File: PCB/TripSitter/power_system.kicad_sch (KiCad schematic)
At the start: 37 parts, among them J4 USB_B_Micro, J5 Jack-DC, SW2 SW_DPDT_x2, SW3 SW_DIP_x05, U2 TPS54325_PWP_14, U5 TPS54294PWP

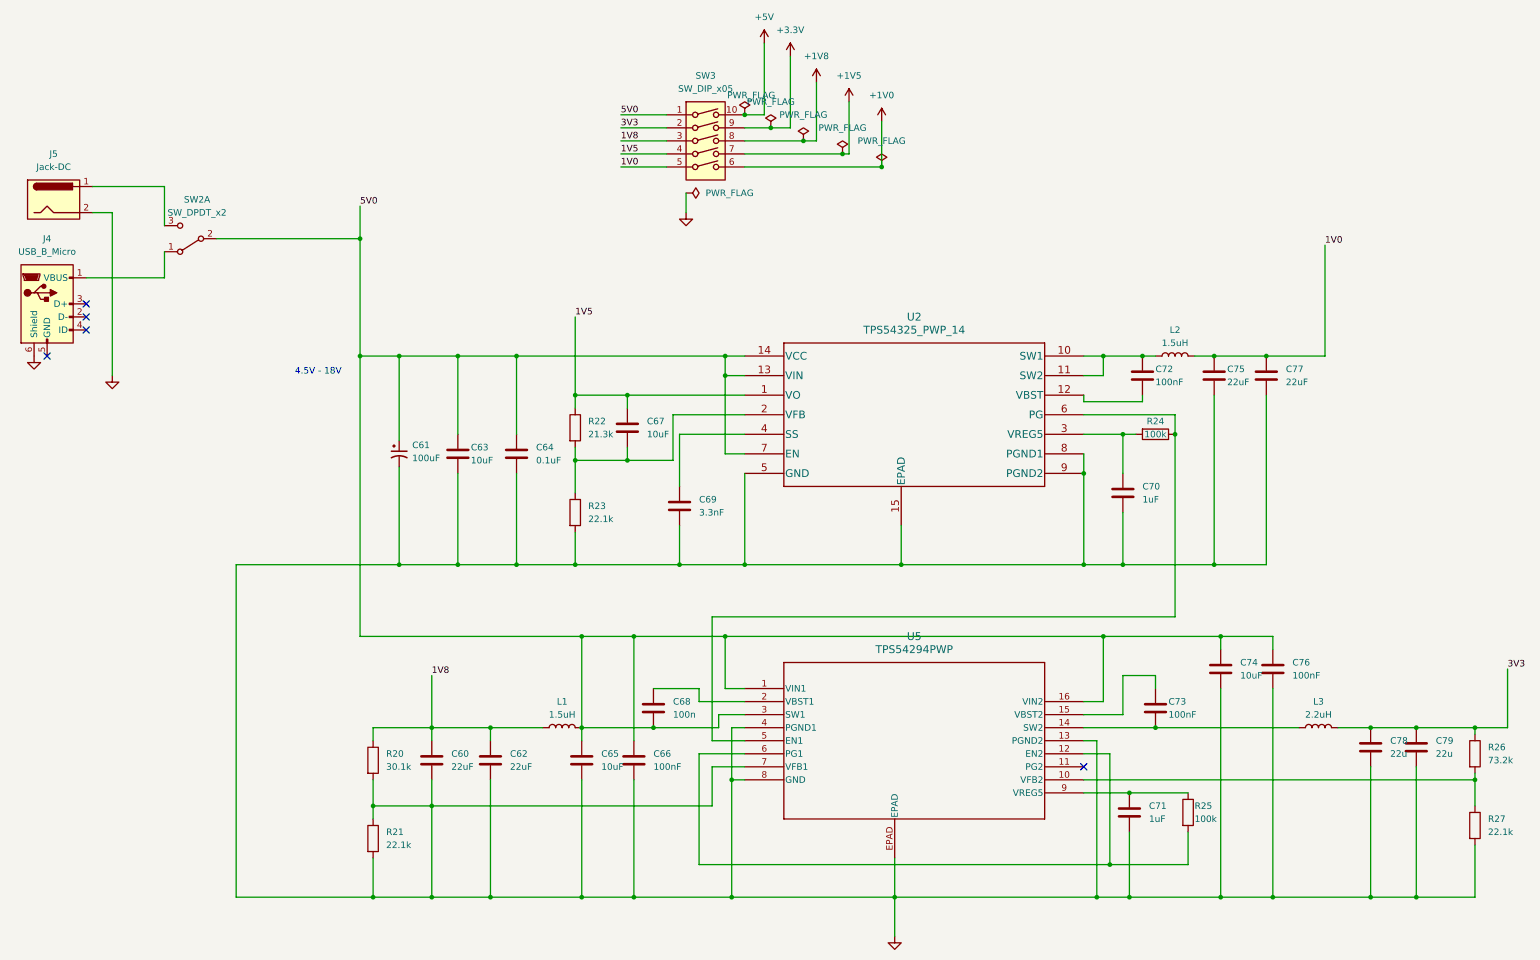
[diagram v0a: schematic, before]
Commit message: pcb: re-structured PCB schematic layout (#17)
Co-authored-by: Sigvart Hovland <sigvart.m@gmail.com>
Co-authored-by: Ida-Sofie Pettersen <idasofie@Ida-Sofies-MacBook-Air.local>
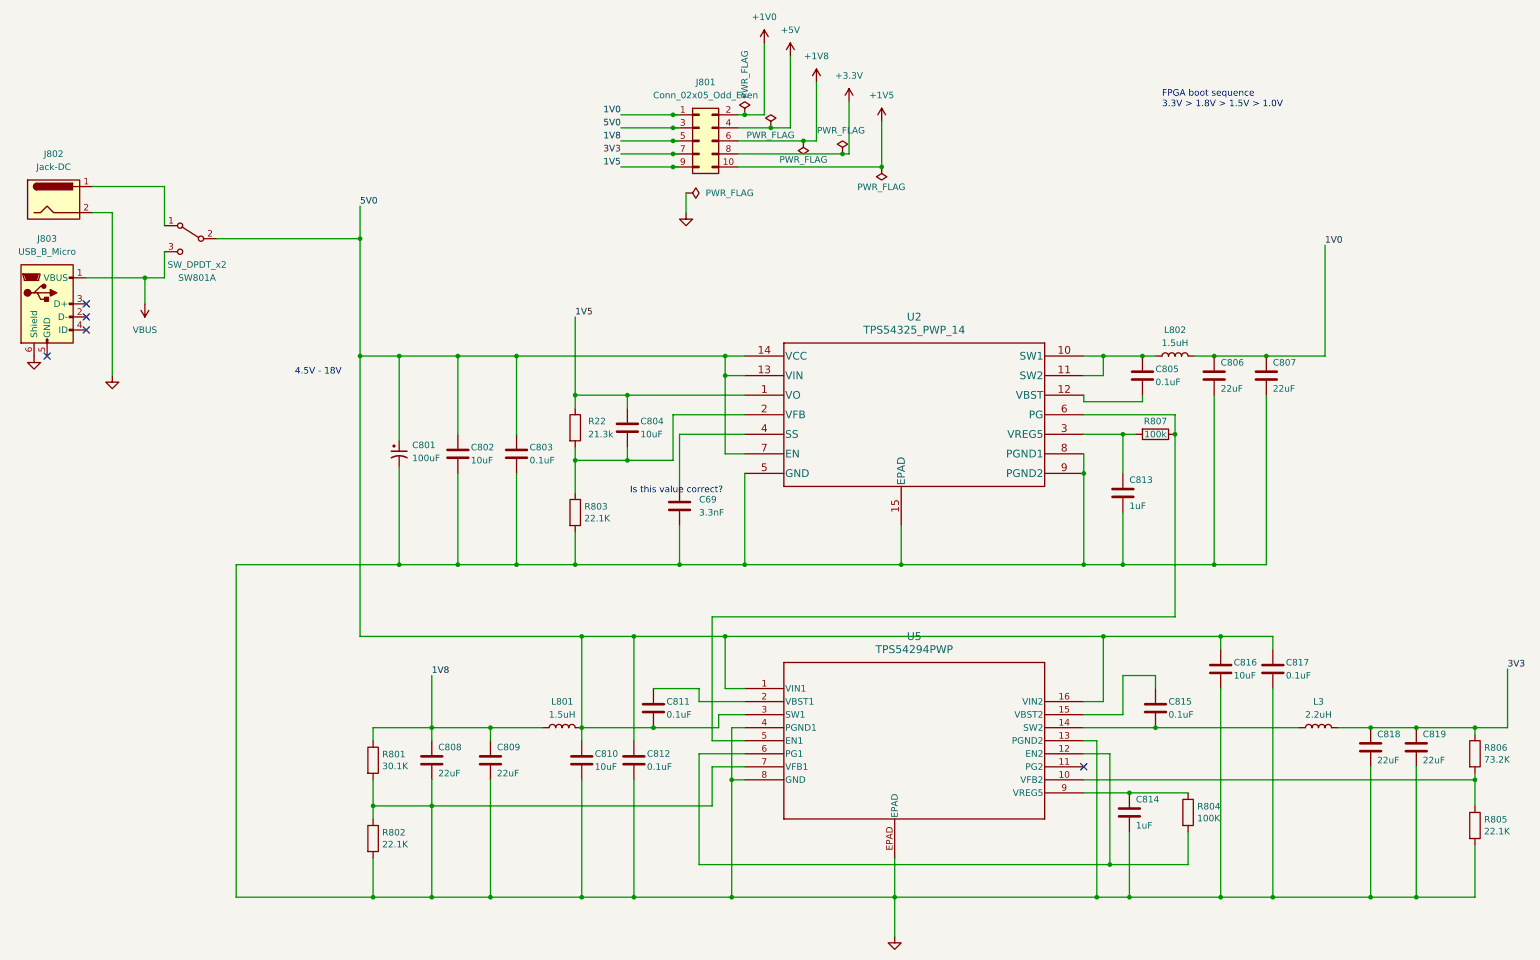
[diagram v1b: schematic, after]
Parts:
- removed C60, C62, C75, C77: 22uF, Capacitor_SMD:C_0402_1005Metric_Pad0.74x0.62mm_HandSolder, symbol Device:C
- removed C64: 0.1uF, Capacitor_SMD:C_0201_0603Metric_Pad0.64x0.40mm_HandSolder, symbol Device:C
- removed C65, C67, C74: 10uF, Capacitor_SMD:C_0402_1005Metric_Pad0.74x0.62mm_HandSolder, symbol Device:C
- removed C66, C72, C73, C76: 100nF, Capacitor_SMD:C_0201_0603Metric_Pad0.64x0.40mm_HandSolder, symbol Device:C
- removed C68: 100n, Capacitor_SMD:C_0201_0603Metric_Pad0.64x0.40mm_HandSolder, symbol Device:C
- removed C70, C71: 1uF, Capacitor_SMD:C_0201_0603Metric_Pad0.64x0.40mm_HandSolder, symbol Device:C
- removed C78, C79: 22u, Capacitor_SMD:C_0402_1005Metric_Pad0.74x0.62mm_HandSolder, symbol Device:C
- removed R20: 30.1k, Resistor_SMD:R_0805_2012Metric_Pad1.20x1.40mm_HandSolder, symbol Device:R
- removed R21, R23, R27: 22.1k, Resistor_SMD:R_0805_2012Metric_Pad1.20x1.40mm_HandSolder, symbol Device:R
- removed R25: 100k, Resistor_SMD:R_0805_2012Metric_Pad1.20x1.40mm_HandSolder, symbol Device:R
- removed R26: 73.2k, Resistor_SMD:R_0805_2012Metric_Pad1.20x1.40mm_HandSolder, symbol Device:R
- removed SW3: SW_DIP_x05, Connector_PinHeader_1.27mm:PinHeader_2x05_P1.27mm_Vertical, symbol Switch:SW_DIP_x05
- added C803, C805, C811, C812, C815, C817: 0.1uF, Capacitor_SMD:C_0603_1608Metric_Pad1.08x0.95mm_HandSolder, symbol Device:C
- added C804, C810, C816: 10uF, Capacitor_SMD:C_0402_1005Metric_Pad0.74x0.62mm_HandSolder, symbol Device:C
- added C806, C807, C808, C809, C818, C819: 22uF, Capacitor_SMD:C_0603_1608Metric_Pad1.08x0.95mm_HandSolder, symbol Device:C
- added C813, C814: 1uF, Capacitor_SMD:C_0402_1005Metric_Pad0.74x0.62mm_HandSolder, symbol Device:C
- added J801: Conn_02x05_Odd_Even, Connector_PinHeader_2.00mm:PinHeader_2x05_P2.00mm_Vertical, symbol Connector_Generic:Conn_02x05_Odd_Even
- added R801: 30.1K, Resistor_SMD:R_0805_2012Metric_Pad1.20x1.40mm_HandSolder, symbol Device:R
- added R802, R803, R805: 22.1K, Resistor_SMD:R_0805_2012Metric_Pad1.20x1.40mm_HandSolder, symbol Device:R
- added R804: 100K, Resistor_SMD:R_0805_2012Metric_Pad1.20x1.40mm_HandSolder, symbol Device:R
- added R806: 73.2K, Resistor_SMD:R_0805_2012Metric_Pad1.20x1.40mm_HandSolder, symbol Device:R
- C69: footprint Capacitor_SMD:C_0402_1005Metric_Pad0.74x0.62mm_HandSolder -> Capacitor_SMD:C_0201_0603Metric_Pad0.64x0.40mm_HandSolder
- C801: renamed from C61; footprint Capacitor_SMD:C_1210_3225Metric_Pad1.33x2.70mm_HandSolder -> Capacitor_SMD:C_0805_2012Metric_Pad1.18x1.45mm_HandSolder; Component Name (none) -> CL21A107MQYNNWE; DK_Ref (none) -> https://www.digikey.no/en/products/detail/samsung-electro-m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
- C802: renamed from C63; Component Name (none) -> CL10A106KQ8NNNC; DK_Ref (none) -> https://www.digikey.no/en/products/detail/samsung-electro-m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
- R807: renamed from R24; Component Name (none) -> RR1220P-104-D; DK_Ref (none) -> https://www.digikey.no/product-detail/no/susumu/RR1220P-104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
- SW801: renamed from SW2; footprint Button_Switch_SMD:SW_DPDT_CK_JS202011JCQN -> Button_Switch_THT:SW_E-Switch_EG1224_SPDT_Angled
- renumbered J5 to J802, J4 to J803, L1 to L801, L2 to L802
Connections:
- net +1V0: now also J801.2 (Pin_2)
- net +1V5: now also J801.10 (Pin_10)
- net +1V8: now also J801.6 (Pin_6)
- net +3.3V: now also J801.8 (Pin_8)
- net +5V: now also J801.4 (Pin_4)
- net 1V0: now also C806.2, C807.2, J801.1 (Pin_1)
- net 1V5: now also C804.1, J801.9 (Pin_9)
- net 1V8: now also C808.2, C809.2, J801.5 (Pin_5), R801.1
- net 3V3: now also C818.2, C819.2, J801.7 (Pin_7), R806.1
- net 5V0: now also C803.1, C810.1, C811.2, C812.1, C816.1, C817.1, J801.3 (Pin_3)
- net GND: now also C803.2, C806.1, C807.1, C808.1, C809.1, C810.2, C812.2, C813.2, C814.2, C816.2, C817.2, C818.1, C819.1, R801.2, R802.1, R802.2, R803.2, R805.2
- net at U5.10 (VFB2): now also R805.1, R806.2
- net at L802.1, U2.10 (SW1), U2.11 (SW2): now also C805.1
- net at U2.12 (VBST): now also C805.2
- net at U5.15 (VBST2): now also C815.1
- net at L3.1, U5.14 (SW2): now also C815.2
- net at U5.12 (EN2), U5.6 (PG1): now also R804.2
- net at U5.2 (VBST1): now also C811.1
- net at U5.9 (VREG5): now also C814.1, R804.1
- net at R22.2, U2.2 (VFB): now also C804.2, R803.1
- net at SW801.1 (A): now also J802.1; no longer J803.1 (VBUS)
- net VBUS: now reaches SW801.3 (C)
- net VBUS: now also J803.1 (VBUS); no longer J802.1
- net at R807.2, U2.3 (VREG5): now also C813.1
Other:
- note added: "FPGA boot sequence 3.3V > 1.8V > 1.5V > 1.0V"
- note added: "Is this value correct?"
- moved on the sheet: SW801A

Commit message: fix power circuit and replace jtag debug
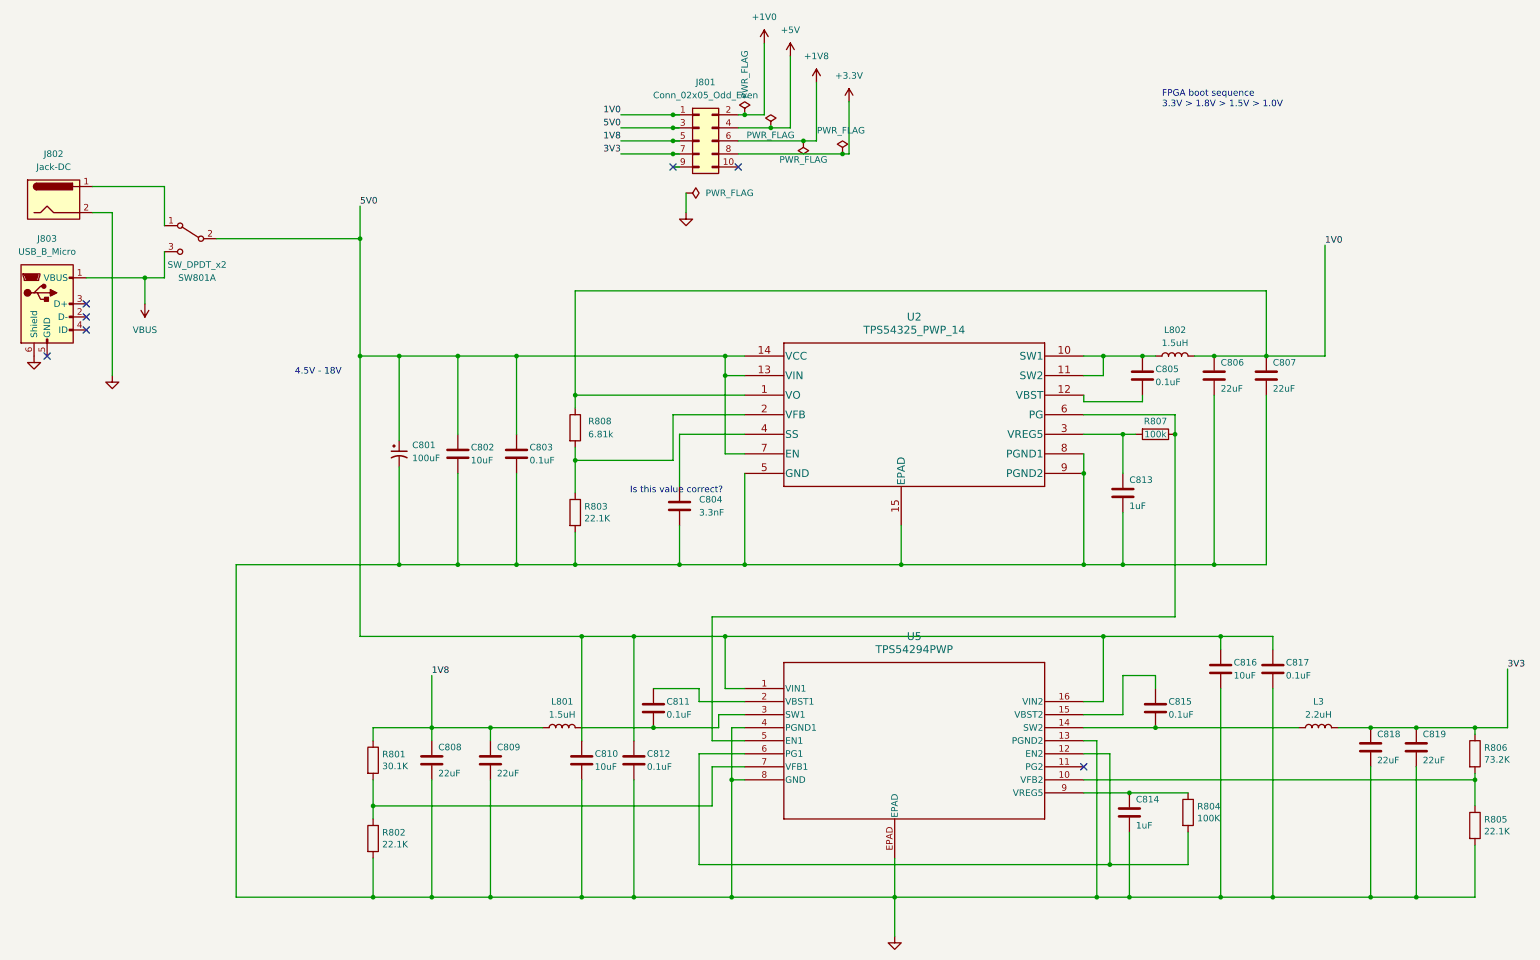
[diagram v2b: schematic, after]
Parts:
- removed C804: 10uF, Capacitor_SMD:C_0402_1005Metric_Pad0.74x0.62mm_HandSolder, symbol Device:C
- R808: renamed from R22; value 21.3k -> 6.81k
- renumbered C69 to C804
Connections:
- net 1V0: now also R808.1, U2.1 (VO)
- net 5V0: no longer C811.2, L801.2, U5.3 (SW1)
- net GND: no longer R801.2, R802.1, U5.7 (VFB1)
- net +1V5: no longer names the net of J801.10 (Pin_10)
- removed net 1V5: J801.9 (Pin_9), R808.1, U2.1 (VO)
- new net: C811.2, L801.2, U5.3 (SW1)
- new net: R801.2, R802.1, U5.7 (VFB1)
- no-connect marks 5 -> 7

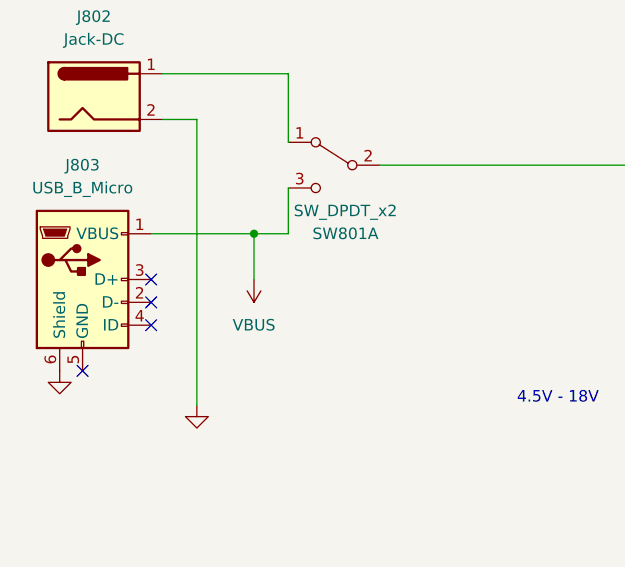
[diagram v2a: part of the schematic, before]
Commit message: fix DRC errors and edit footprint vias
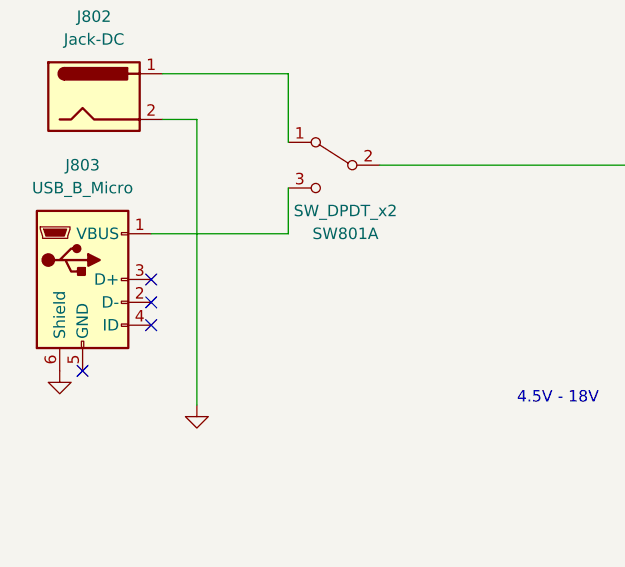
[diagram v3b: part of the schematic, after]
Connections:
- net VBUS: no longer names the net of J803.1 (VBUS), SW801.3 (C)
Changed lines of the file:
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@@
   (junction (at 224.79 217.17) (diameter 0) (color 0 0 0 0)
-  )
-  (junction (at 78.74 96.52) (diameter 0) (color 0 0 0 0)
   )
   (junction (at 317.5 184.15) (diameter 0) (color 0 0 0 0)
@@
     (stroke (width 0) (type default))
   )
-  (wire (pts (xy 67.31 96.52) (xy 78.74 96.52))
-    (stroke (width 0) (type default))
-  )
-  (wire (pts (xy 78.74 96.52) (xy 82.55 96.52))
+  (wire (pts (xy 67.31 96.52) (xy 82.55 96.52))
     (stroke (width 0) (type default))
   )
@@
   )
   (wire (pts (xy 123.19 217.17) (xy 134.62 217.17))
-    (stroke (width 0) (type default))
-  )
-  (wire (pts (xy 78.74 96.52) (xy 78.74 101.6))
     (stroke (width 0) (type default))
   )
@@
         )
       )
-    )
-  )
-  (symbol (lib_id "power:VBUS") (at 78.74 101.6 180) (unit 1)
-    (in_bom yes) (on_board yes) (dnp no) (fields_autoplaced)
-    (property "Reference" "#PWR047" (at 78.74 97.79 0)
-      (effects (font (size 1.27 1.27)) hide)
-    )
-    (property "Value" "VBUS" (at 78.74 106.68 0)
-      (effects (font (size 1.27 1.27)))
-    )
-    (property "Footprint" "" (at 78.74 101.6 0)
-      (effects (font (size 1.27 1.27)) hide)
-    )
-    (property "Datasheet" "" (at 78.74 101.6 0)
-      (effects (font (size 1.27 1.27)) hide)
-    )
-    (pin "1")
-    (instances
-      (project "TripSitter"
-        (path "/5ab65702-9689-4dfd-8f10-6407062323a6/87bcf595-d251-4aa5-8b35-efc055826b19/750eb09f-8f96-43e9-bfb8-1e6e7cd9bea9"
-          (reference "#PWR047") (unit 1)
-        )
-        (path "/5ab65702-9689-4dfd-8f10-6407062323a6/8ae76c2e-e928-4bfb-9cc2-9dfcb5e6a658"
-          (reference "#PWR071") (unit 1)
-        )
-      )
